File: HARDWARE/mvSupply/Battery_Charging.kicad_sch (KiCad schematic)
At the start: 1 part

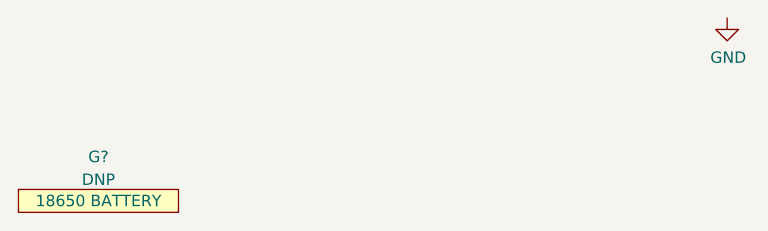
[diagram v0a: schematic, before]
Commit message: Testing submodule retrieval
Committing to see if it will grab latest library commit
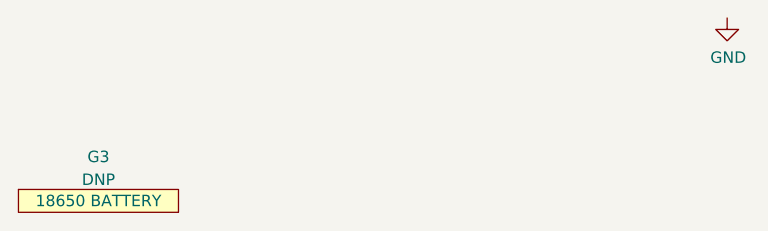
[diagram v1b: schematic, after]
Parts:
- gave numbers to parts that had none: 1
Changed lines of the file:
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@@
   (symbol (lib_id "master-vampire:G") (at 76.2 96.52 0) (unit 1)
     (in_bom yes) (on_board yes) (fields_autoplaced)
-    (property "Reference" "G?" (id 0) (at 76.2 91.6264 0))
+    (property "Reference" "G3" (id 0) (at 76.2 91.6264 0))
     (property "Value" "18650 BATTERY" (id 1) (at 76.2 96.52 0))
     (property "Footprint" "" (id 2) (at 76.2 96.52 0)
